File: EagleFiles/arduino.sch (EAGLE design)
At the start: 16 parts, among them IC1 ATMEGA328", IC2 74250N, IC3 74250N, IC4 74250N, IC5 3.3V, IC6 4053D

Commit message: fixed the i2c stuff
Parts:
- removed IC6: 4053D, 40xx:4053D
- added C5: 0.22, SparkFun:CAP0402-CAP
- added C6: 0.1, SparkFun:CAP0402-CAP
- added C7: (no value), SparkFun:CAP0402-CAP
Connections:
- removed net N$41 (its old number): IC1.(PCI12/ADC4/SDA)PC4, IC6A.A
- removed net VCC: IC2A.G
- new net N$62: 3-AXIS_MAG.C1, C7.2
- net GND: now also C6.1, C7.1, IC2A.G
- net N$43: now also 3-AXIS_GYRO.SDA, IC1.(PCI12/ADC4/SDA)PC4; no longer IC1.(PCI19/INT1/OC2B)PD3
- net N$44: now also 3-AXIS_MAG.SETC, C5.1; no longer 3-AXIS_MAG.SDA, IC6A.Z0
- net N$45: now also 3-AXIS_MAG.SETP, C5.2; no longer 3-AXIS_GYRO.SDA, IC6A.Z1
- net N$67: now also C6.2
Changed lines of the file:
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@@
 <part name="IC3" library="74xx-eu" deviceset="74*250" device="N"/>
 <part name="SUPPLY2" library="supply2" deviceset="GND" device=""/>
-<part name="P+1" library="supply1" deviceset="VCC" device=""/>
 <part name="JP1" library="RBBB" deviceset="1X16_HEADER" device="&quot;"/>
 <part name="JP2" library="RBBB" deviceset="1X16_HEADER" device="&quot;"/>
@@
 <part name="C4" library="SparkFun" deviceset="CAP" device="PTH" value="2.2 nF"/>
 <part name="IC5" library="RBBB" deviceset="REGULATOR" device="" value="3.3V"/>
-<part name="IC6" library="40xx" deviceset="4053" device="D"/>
+<part name="SUPPLY3" library="supply2" deviceset="GND" device=""/>
+<part name="C5" library="SparkFun" deviceset="CAP" device="0402-CAP" value="0.22"/>
+<part name="C6" library="SparkFun" deviceset="CAP" device="0402-CAP" value="0.1"/>
+<part name="C7" library="SparkFun" deviceset="CAP" device="0402-CAP"/>
 </parts>
 <sheets>
@@
 <instance part="IC3" gate="A" x="210.82" y="2.54" rot="R180"/>
 <instance part="SUPPLY2" gate="GND" x="154.94" y="27.94"/>
-<instance part="P+1" gate="VCC" x="177.8" y="101.6"/>
 <instance part="JP1" gate="G$1" x="241.3" y="63.5" rot="R180"/>
 <instance part="JP2" gate="G$1" x="241.3" y="-5.08" rot="R180"/>
@@
 <instance part="C4" gate="G$1" x="81.28" y="-40.64"/>
 <instance part="IC5" gate="1" x="66.04" y="-7.62"/>
-<instance part="IC6" gate="A" x="104.14" y="-81.28" rot="R180"/>
+<instance part="SUPPLY3" gate="GND" x="154.94" y="96.52"/>
+<instance part="C5" gate="G$1" x="116.84" y="7.62"/>
+<instance part="C6" gate="G$1" x="71.12" y="12.7" rot="R90"/>
+<instance part="C7" gate="G$1" x="71.12" y="7.62" rot="R90"/>
 </instances>
 <busses>
@@
 <wire x1="121.92" y1="-33.02" x2="121.92" y2="-40.64" width="0.1524" layer="91"/>
 <pinref part="3-AXIS_MAG" gate="G$1" pin="GND"/>
-<wire x1="83.82" y1="17.78" x2="38.1" y2="17.78" width="0.1524" layer="91"/>
+<wire x1="83.82" y1="17.78" x2="66.04" y2="17.78" width="0.1524" layer="91"/>
 <junction x="38.1" y="17.78"/>
+<pinref part="C6" gate="G$1" pin="1"/>
+<wire x1="66.04" y1="17.78" x2="38.1" y2="17.78" width="0.1524" layer="91"/>
+<wire x1="66.04" y1="12.7" x2="66.04" y2="17.78" width="0.1524" layer="91"/>
+<junction x="66.04" y="17.78"/>
+<pinref part="C7" gate="G$1" pin="1"/>
+<wire x1="66.04" y1="7.62" x2="66.04" y2="12.7" width="0.1524" layer="91"/>
+<junction x="66.04" y="12.7"/>
 </segment>
 <segment>
@@
 <pinref part="SUPPLY1" gate="GND" pin="GND"/>
 <wire x1="223.52" y1="-45.72" x2="160.02" y2="-45.72" width="0.1524" layer="91"/>
+</segment>
+<segment>
+<pinref part="IC2" gate="A" pin="G"/>
+<wire x1="220.98" y1="99.06" x2="154.94" y2="99.06" width="0.1524" layer="91"/>
+<pinref part="SUPPLY3" gate="GND" pin="GND"/>
 </segment>
 </net>
@@
 </segment>
 </net>
-<net name="VCC" class="0">
-<segment>
-<pinref part="IC2" gate="A" pin="G"/>
-<wire x1="220.98" y1="99.06" x2="177.8" y2="99.06" width="0.1524" layer="91"/>
-<pinref part="P+1" gate="VCC" pin="VCC"/>
-</segment>
-</net>
 <net name="N$7" class="0">
 <segment>
@@
 <pinref part="JP3" gate="G$1" pin="16"/>
 <wire x1="223.52" y1="-104.14" x2="233.68" y2="-104.14" width="0.1524" layer="91"/>
-</segment>
-</net>
-<net name="N$62" class="0">
-<segment>
-<pinref part="3-AXIS_GYRO" gate="G$1" pin="SCL"/>
-<wire x1="119.38" y1="-25.4" x2="124.46" y2="-25.4" width="0.1524" layer="91"/>
-<wire x1="124.46" y1="-25.4" x2="124.46" y2="22.86" width="0.1524" layer="91"/>
-<pinref part="IC1" gate="G$1" pin="(PCI13/ADC5/SCL)PC5"/>
-<wire x1="124.46" y1="22.86" x2="124.46" y2="86.36" width="0.1524" layer="91"/>
-<wire x1="124.46" y1="86.36" x2="119.38" y2="86.36" width="0.1524" layer="91"/>
-<pinref part="3-AXIS_MAG" gate="G$1" pin="SCL"/>
-<wire x1="114.3" y1="22.86" x2="124.46" y2="22.86" width="0.1524" layer="91"/>
-<junction x="124.46" y="22.86"/>
 </segment>
 </net>
@@
 <junction x="76.2" y="-7.62"/>
 <junction x="81.28" y="22.86"/>
+<wire x1="81.28" y1="20.32" x2="81.28" y2="12.7" width="0.1524" layer="91"/>
+<wire x1="81.28" y1="12.7" x2="86.36" y2="12.7" width="0.1524" layer="91"/>
+<junction x="81.28" y="20.32"/>
+<wire x1="81.28" y1="12.7" x2="73.66" y2="12.7" width="0.1524" layer="91"/>
+<junction x="81.28" y="12.7"/>
+<pinref part="C6" gate="G$1" pin="2"/>
 </segment>
 </net>
 <net name="N$41" class="0">
 <segment>
-<pinref part="IC6" gate="A" pin="A"/>
-<wire x1="116.84" y1="-71.12" x2="139.7" y2="-71.12" width="0.1524" layer="91"/>
-<wire x1="139.7" y1="-71.12" x2="139.7" y2="88.9" width="0.1524" layer="91"/>
+<pinref part="3-AXIS_MAG" gate="G$1" pin="SCL"/>
+<wire x1="114.3" y1="22.86" x2="127" y2="22.86" width="0.1524" layer="91"/>
+<wire x1="127" y1="22.86" x2="127" y2="86.36" width="0.1524" layer="91"/>
+<pinref part="IC1" gate="G$1" pin="(PCI13/ADC5/SCL)PC5"/>
+<wire x1="127" y1="86.36" x2="119.38" y2="86.36" width="0.1524" layer="91"/>
+<pinref part="3-AXIS_GYRO" gate="G$1" pin="SCL"/>
+<wire x1="119.38" y1="-25.4" x2="127" y2="-25.4" width="0.1524" layer="91"/>
+<wire x1="127" y1="-25.4" x2="127" y2="22.86" width="0.1524" layer="91"/>
+<junction x="127" y="22.86"/>
+</segment>
+</net>
+<net name="N$43" class="0">
+<segment>
 <pinref part="IC1" gate="G$1" pin="(PCI12/ADC4/SDA)PC4"/>
-<wire x1="139.7" y1="88.9" x2="119.38" y2="88.9" width="0.1524" layer="91"/>
-</segment>
-</net>
-<net name="N$43" class="0">
-<segment>
-<wire x1="86.36" y1="-96.52" x2="86.36" y2="-58.42" width="0.1524" layer="91"/>
-<wire x1="86.36" y1="-58.42" x2="137.16" y2="-58.42" width="0.1524" layer="91"/>
-<wire x1="137.16" y1="-58.42" x2="137.16" y2="66.04" width="0.1524" layer="91"/>
-<pinref part="IC1" gate="G$1" pin="(PCI19/INT1/OC2B)PD3"/>
-<wire x1="137.16" y1="66.04" x2="119.38" y2="66.04" width="0.1524" layer="91"/>
-<wire x1="86.36" y1="-96.52" x2="93.98" y2="-96.52" width="0.1524" layer="91"/>
+<wire x1="119.38" y1="88.9" x2="132.08" y2="88.9" width="0.1524" layer="91"/>
+<wire x1="132.08" y1="88.9" x2="132.08" y2="17.78" width="0.1524" layer="91"/>
+<wire x1="111.76" y1="17.78" x2="132.08" y2="17.78" width="0.1524" layer="91"/>
+<wire x1="132.08" y1="17.78" x2="132.08" y2="-20.32" width="0.1524" layer="91"/>
+<pinref part="3-AXIS_GYRO" gate="G$1" pin="SDA"/>
+<wire x1="132.08" y1="-20.32" x2="119.38" y2="-20.32" width="0.1524" layer="91"/>
+<junction x="132.08" y="17.78"/>
 </segment>
 </net>
 <net name="N$44" class="0">
 <segment>
-<pinref part="3-AXIS_MAG" gate="G$1" pin="SDA"/>
-<wire x1="114.3" y1="17.78" x2="134.62" y2="17.78" width="0.1524" layer="91"/>
-<wire x1="134.62" y1="17.78" x2="134.62" y2="-81.28" width="0.1524" layer="91"/>
-<pinref part="IC6" gate="A" pin="Z0"/>
-<wire x1="134.62" y1="-81.28" x2="116.84" y2="-81.28" width="0.1524" layer="91"/>
+<pinref part="3-AXIS_MAG" gate="G$1" pin="SETC"/>
+<pinref part="C5" gate="G$1" pin="1"/>
+<wire x1="114.3" y1="12.7" x2="116.84" y2="12.7" width="0.1524" layer="91"/>
 </segment>
 </net>
 <net name="N$45" class="0">
 <segment>
-<pinref part="3-AXIS_GYRO" gate="G$1" pin="SDA"/>
-<wire x1="119.38" y1="-20.32" x2="132.08" y2="-20.32" width="0.1524" layer="91"/>
-<wire x1="132.08" y1="-20.32" x2="132.08" y2="-78.74" width="0.1524" layer="91"/>
-<pinref part="IC6" gate="A" pin="Z1"/>
-<wire x1="132.08" y1="-78.74" x2="116.84" y2="-78.74" width="0.1524" layer="91"/>
-</segment>
-</net>
+<pinref part="C5" gate="G$1" pin="2"/>
+<pinref part="3-AXIS_MAG" gate="G$1" pin="SETP"/>
+<wire x1="116.84" y1="5.08" x2="114.3" y2="5.08" width="0.1524" layer="91"/>
+<wire x1="114.3" y1="5.08" x2="114.3" y2="10.16" width="0.1524" layer="91"/>
+</segment>
+</net>
+<net name="N$62" class="0">
+<segment>
+<pinref part="3-AXIS_MAG" gate="G$1" pin="C1"/>
+<wire x1="83.82" y1="10.16" x2="81.28" y2="10.16" width="0.1524" layer="91"/>
+<wire x1="81.28" y1="10.16" x2="81.28" y2="7.62" width="0.1524" layer="91"/>
+<pinref part="C7" gate="G$1" pin="2"/>
+<wire x1="81.28" y1="7.62" x2="73.66" y2="7.62" width="0.1524" layer="91"/>
+</segment>
+</net>

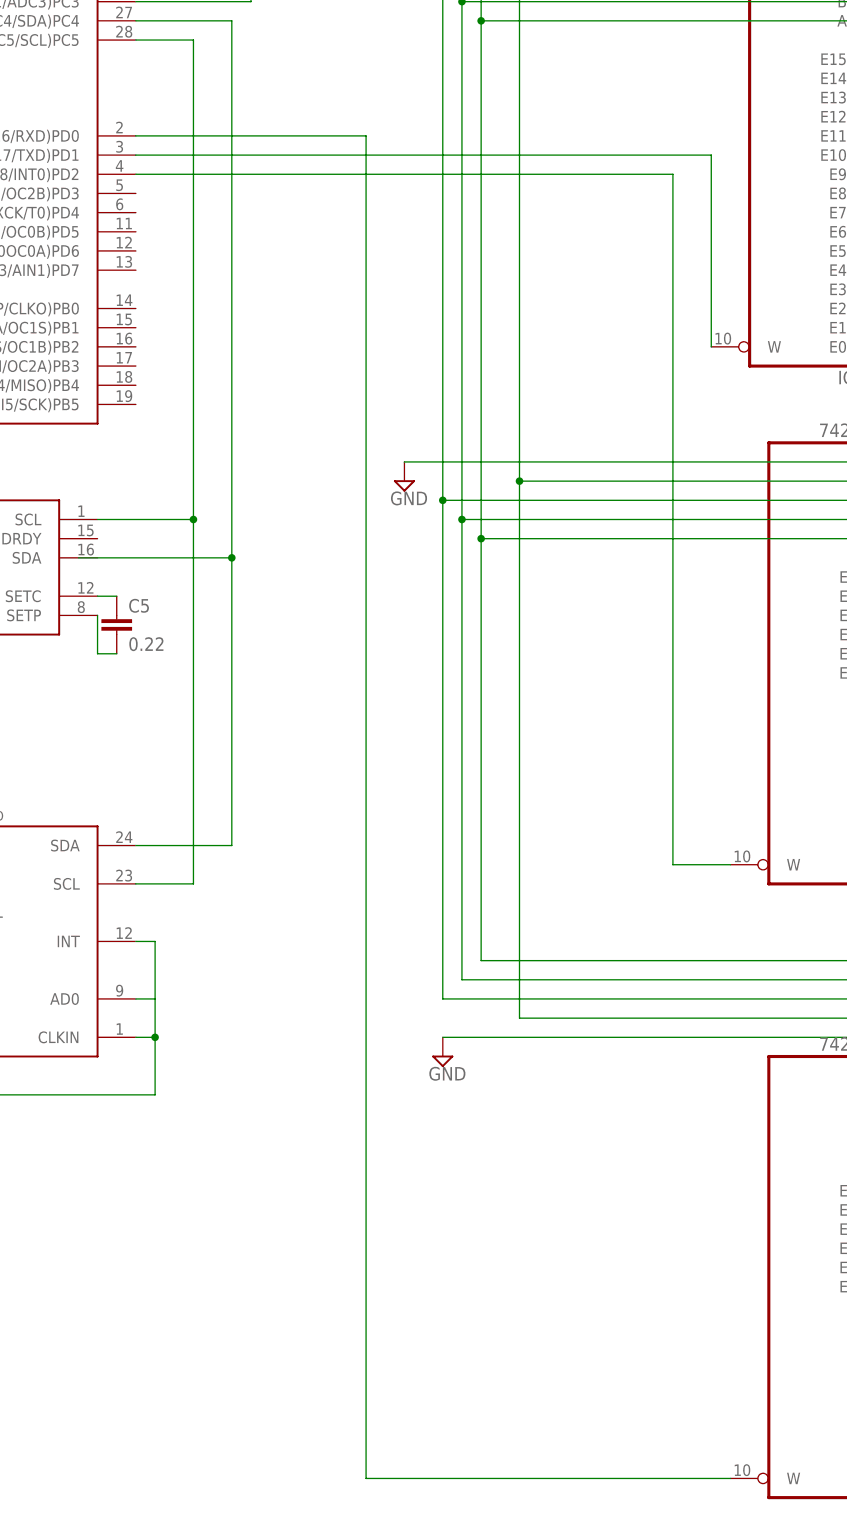
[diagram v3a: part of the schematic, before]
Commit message: removed mux connection to rx and tx
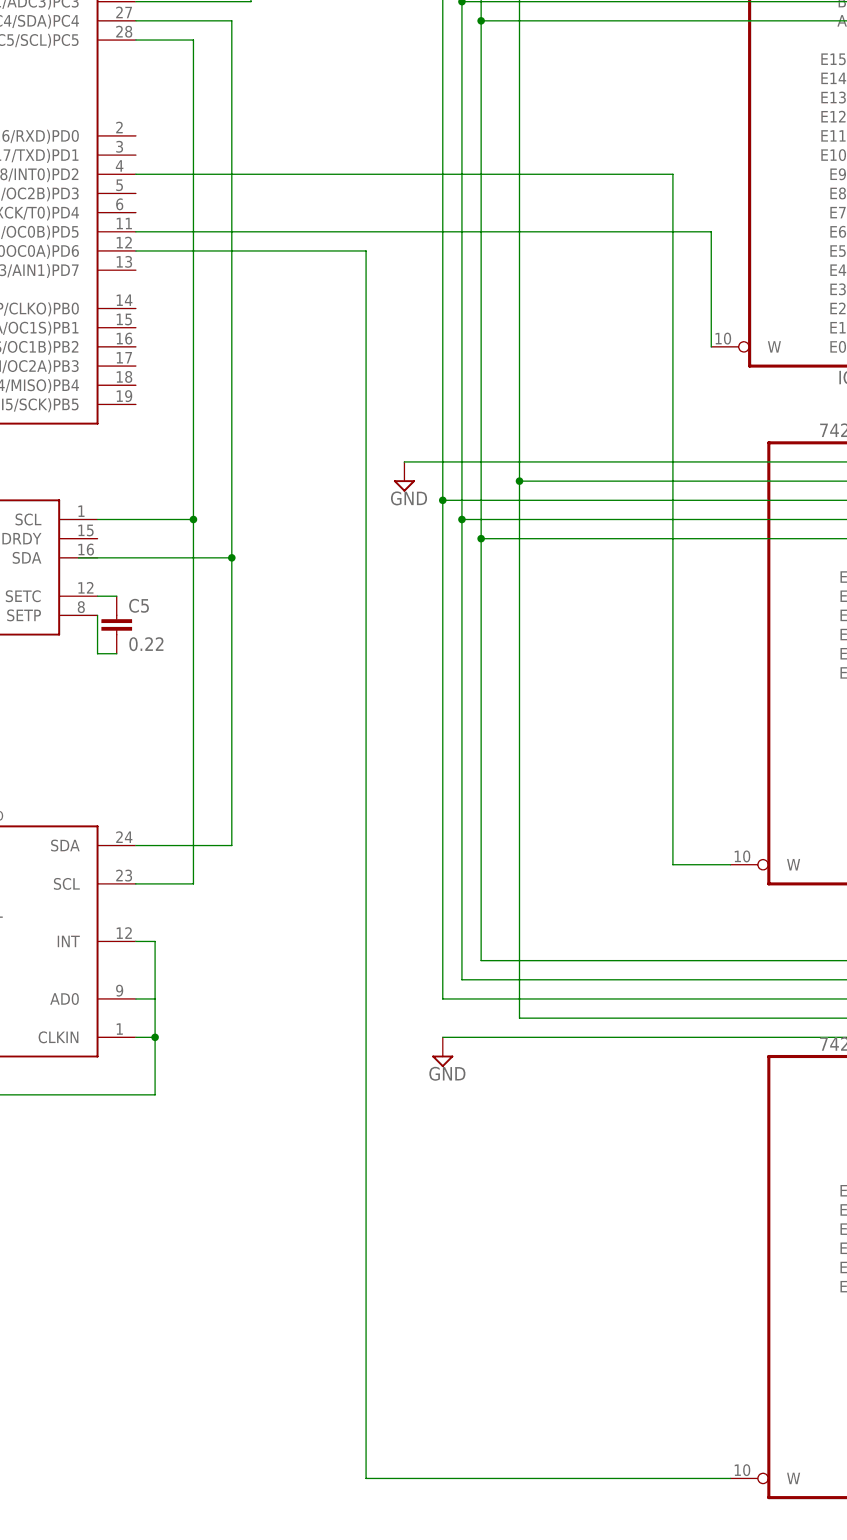
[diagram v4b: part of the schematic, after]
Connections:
- net N$42: now also IC1.(PCI22/AIN0OC0A)PD6; no longer IC1.(PCI16/RXD)PD0
- net N$5: now also IC1.(PCI21/T1/OC0B)PD5; no longer IC1.(PCI17/TXD)PD1
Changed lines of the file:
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@@
 <segment>
 <pinref part="IC2" gate="A" pin="W"/>
-<wire x1="195.58" y1="45.72" x2="195.58" y2="71.12" width="0.1524" layer="91"/>
-<pinref part="IC1" gate="G$1" pin="(PCI17/TXD)PD1"/>
-<wire x1="119.38" y1="71.12" x2="195.58" y2="71.12" width="0.1524" layer="91"/>
+<wire x1="195.58" y1="45.72" x2="195.58" y2="60.96" width="0.1524" layer="91"/>
+<pinref part="IC1" gate="G$1" pin="(PCI21/T1/OC0B)PD5"/>
+<wire x1="119.38" y1="60.96" x2="195.58" y2="60.96" width="0.1524" layer="91"/>
 </segment>
 </net>
@@
 <pinref part="IC4" gate="A" pin="W"/>
 <wire x1="198.12" y1="-104.14" x2="149.86" y2="-104.14" width="0.1524" layer="91"/>
-<wire x1="149.86" y1="-104.14" x2="149.86" y2="73.66" width="0.1524" layer="91"/>
-<pinref part="IC1" gate="G$1" pin="(PCI16/RXD)PD0"/>
-<wire x1="149.86" y1="73.66" x2="119.38" y2="73.66" width="0.1524" layer="91"/>
-</segment>
-</net>
+<wire x1="149.86" y1="-104.14" x2="149.86" y2="58.42" width="0.1524" layer="91"/>
+<pinref part="IC1" gate="G$1" pin="(PCI22/AIN0OC0A)PD6"/>
+<wire x1="119.38" y1="58.42" x2="149.86" y2="58.42" width="0.1524" layer="91"/>
+</segment>
+</net>
